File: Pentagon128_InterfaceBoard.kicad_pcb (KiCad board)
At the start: 2 copper layers, 150 x 121.6 mm, 40 parts, among them J1 DIN41612_02x32_AB, J10 Tape Out, J11 Tape In, J12 Mini-DIN-6, J14 Barrel_Jack_Switch, J2 Conn_02x03_Odd_Even ATmega Pr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, J3 Conn_02x08_Odd_Even Ext Keyb, J4 Conn_02x05_Odd_Even Kempston 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, J5 DE9_Plug Kempston Out SMD, J6 DE15_Plug_HighDensity VGA CRT, J7 Conn_01x04 FDD Power, J8 Conn_01x04 Audio In, J9 AudioJack3, Q1 Q_NPN_BCE, Q2 Q_NPN_BCE, Q3 Q_NPN_BCE, Q4 Q_NPN_BCE, U1 MT8816 PLCC44, U2 ATmega168PA-A

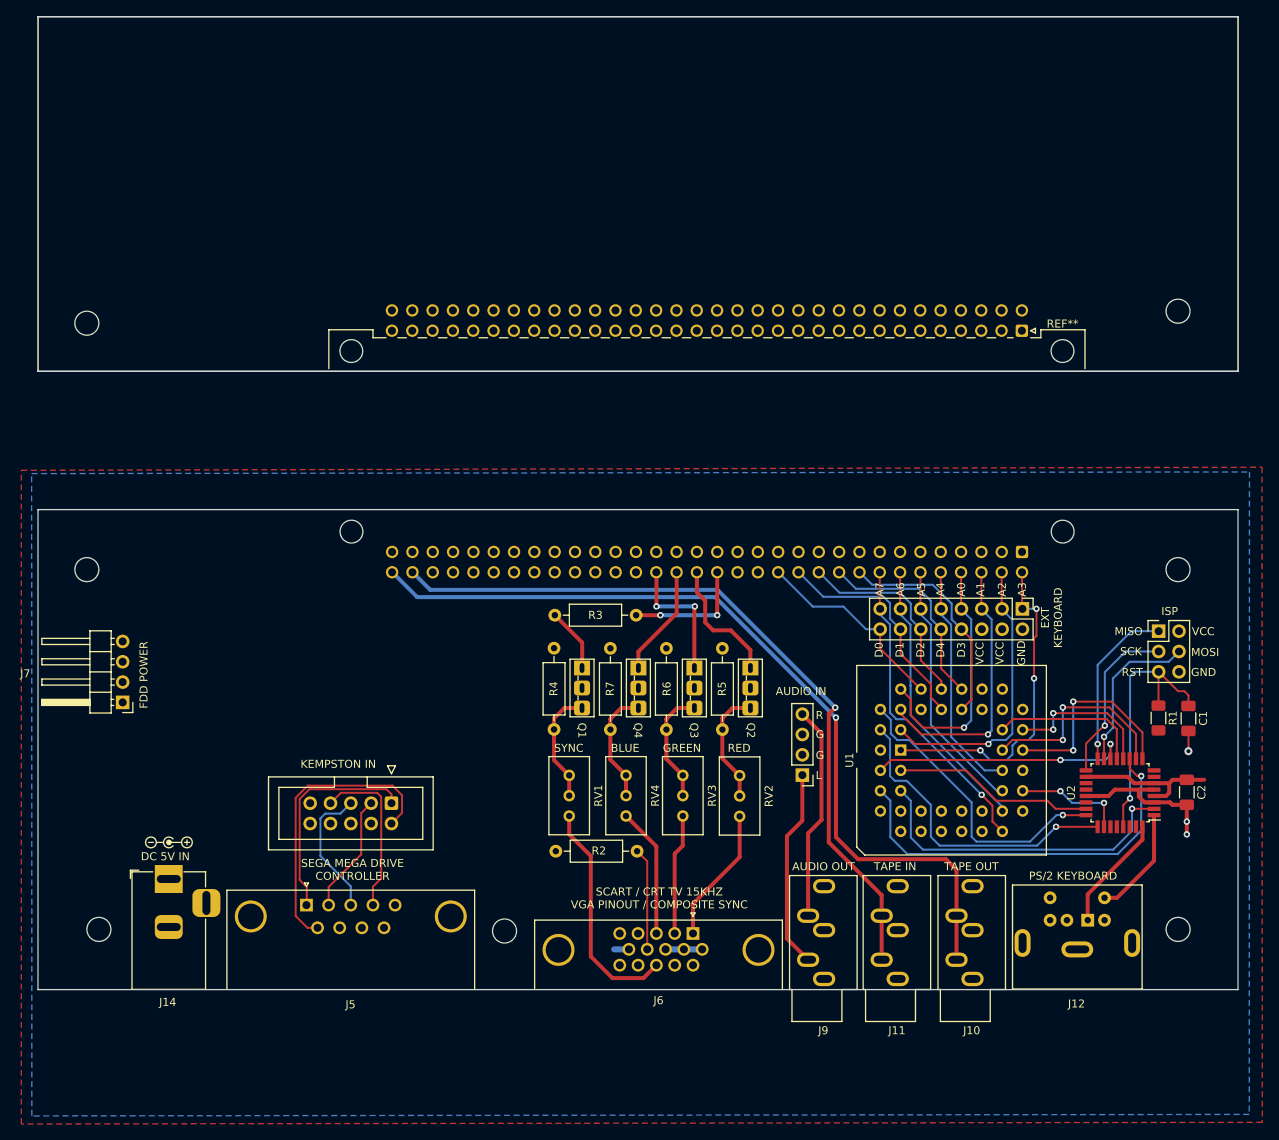
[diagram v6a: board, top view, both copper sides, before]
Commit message: Add VGA output based on @Alex_Eburg's https://github.com/AlexEkb4ever/ZX_RGBI2VGA-HDMI Repace Raspberry Pi Pico with RP2040-Zero. Add 9 pin RGBI header for Pentagon 2023. Add RP2040-Zero symbol and footprint.
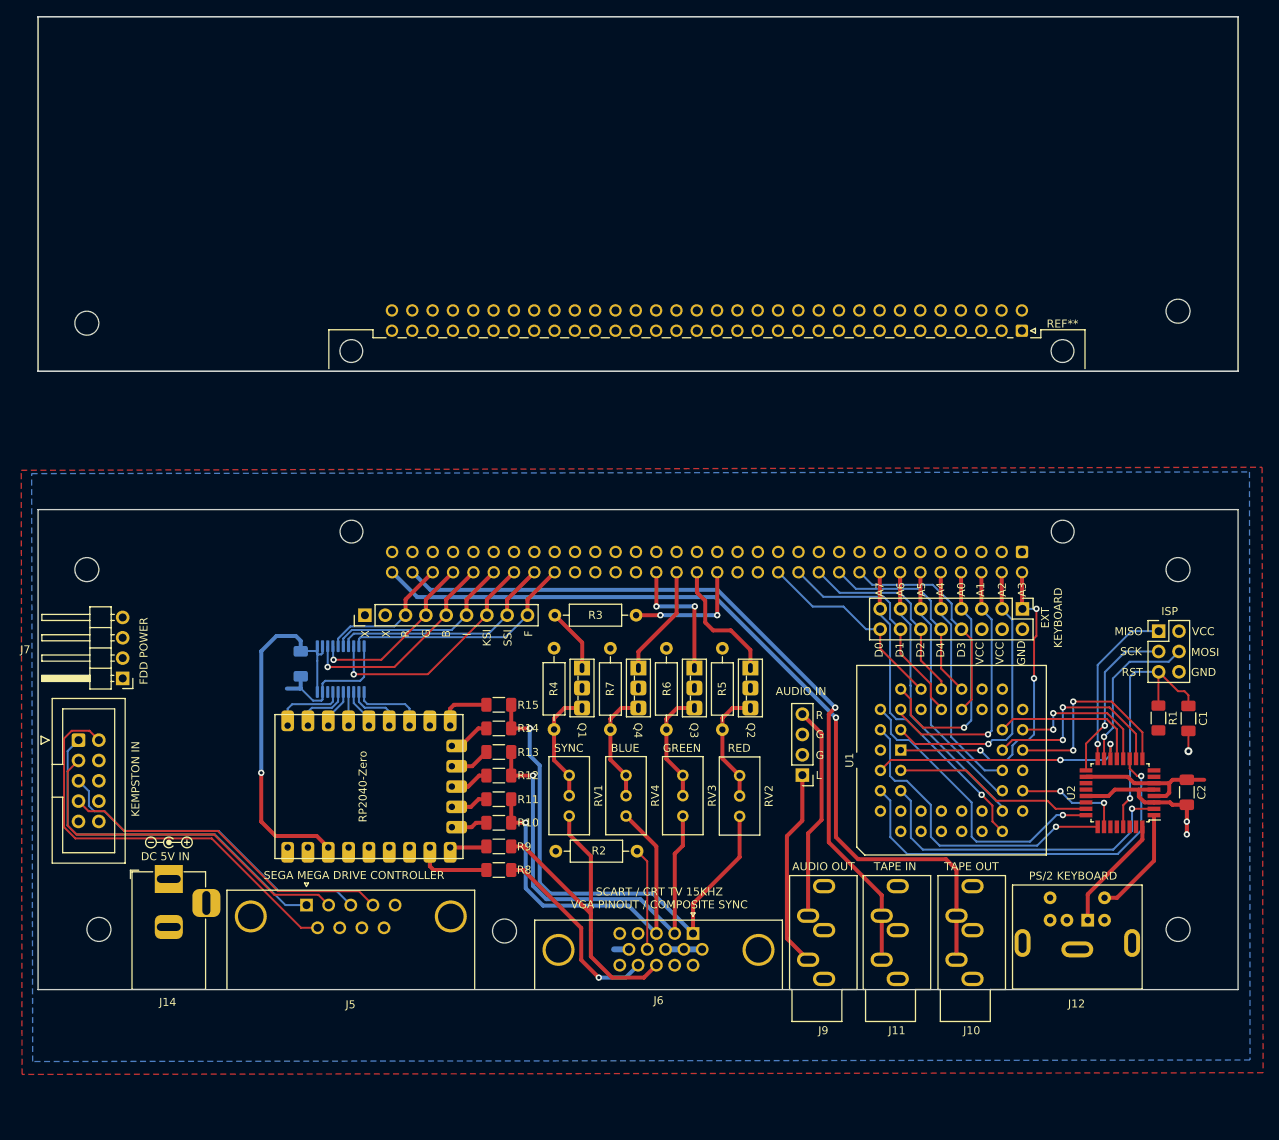
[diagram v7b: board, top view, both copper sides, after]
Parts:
- added C6: 0.1uF, Capacitor_SMD:C_1206_3216Metric_Pad1.33x1.80mm_HandSolder, B.Cu at (87.4, 77.6)
- added J15: Conn_01x07, Connector_PinHeader_2.54mm:PinHeader_1x09_P2.54mm_Vertical, F.Cu at (95.5, 71.5)
- added R10: 390, Resistor_SMD:R_1206_3216Metric_Pad1.30x1.75mm_HandSolder, F.Cu at (112.2, 97.5)
- added R11: 820, Resistor_SMD:R_1206_3216Metric_Pad1.30x1.75mm_HandSolder, F.Cu at (112.2, 94.5)
- added R12: 390, Resistor_SMD:R_1206_3216Metric_Pad1.30x1.75mm_HandSolder, F.Cu at (112.2, 91.5)
- added R13: 820, Resistor_SMD:R_1206_3216Metric_Pad1.30x1.75mm_HandSolder, F.Cu at (112.2, 88.6)
- added R14: 390, Resistor_SMD:R_1206_3216Metric_Pad1.30x1.75mm_HandSolder, F.Cu at (112.2, 85.7)
- added R15: 820, Resistor_SMD:R_1206_3216Metric_Pad1.30x1.75mm_HandSolder, F.Cu at (112.2, 82.7)
- added R8: 100, Resistor_SMD:R_1206_3216Metric_Pad1.30x1.75mm_HandSolder, F.Cu at (112.2, 103.3)
- added R9: 100, Resistor_SMD:R_1206_3216Metric_Pad1.30x1.75mm_HandSolder, F.Cu at (112.2, 100.4)
- added RZ1: RP2040-Zero, RP2040-Zero:RP2040-Zero, F.Cu at (108.7, 103.1)
- added U3: 74HC245, Package_SO:TSSOP-20_4.4x6.5mm_P0.65mm, B.Cu at (92.4, 78.2)
- moved J4 39.9 mm to (59.7, 87.1), turned to 0 degrees
- moved J7 3.00 mm to (65.2, 79.4)
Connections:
- net /CRT_BLUE renamed CRT_BLUE
- net /CRT_GREEN renamed CRT_GREEN
- net /CRT_RED renamed CRT_RED
- net /CRT_SYNC renamed CRT_SYNC
- J1 pad b24: unconnected-(J1-Pin_b24-Padb24) -> F
- J1 pad b25: unconnected-(J1-Pin_b25-Padb25) -> SSI
- J1 pad b26: unconnected-(J1-Pin_b26-Padb26) -> KSI
- J1 pad b27: unconnected-(J1-Pin_b27-Padb27) -> I
- J1 pad b28: unconnected-(J1-Pin_b28-Padb28) -> B
- J1 pad b29: unconnected-(J1-Pin_b29-Padb29) -> G
- J1 pad b30: unconnected-(J1-Pin_b30-Padb30) -> R
- J6 pad 14: unconnected-(J6-Pad14) -> CRT_VSYNC
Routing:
- net /pico RGB TO VGA/3V3: track 0.00 -> 47.8 mm, vias 0 -> 1
- net CRT_RED: track 17.1 -> 64.0 mm, vias 0 -> 1
- net CRT_GREEN: track 15.1 -> 54.8 mm, vias 0 -> 1
- net CRT_BLUE: track 16.2 -> 47.8 mm, vias 0 -> 1
- net /DOWN: track 14.9 -> 45.4 mm
- net KSI: track 0.00 -> 30.0 mm, vias 0 -> 1
- net F: track 0.00 -> 30.0 mm
- net SSI: track 0.00 -> 28.7 mm
- net B: track 0.00 -> 26.9 mm, vias 0 -> 1
- net /LEFT: track 17.0 -> 41.6 mm
- net CRT_VSYNC: track 0.00 -> 24.4 mm, vias 0 -> 1
- net I: track 0.00 -> 24.3 mm
- net G: track 0.00 -> 22.4 mm, vias 0 -> 1
- net /RIGHT: track 21.0 -> 42.2 mm
- net /UP: track 27.0 -> 45.3 mm
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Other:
- board text added: "B"
- board text added: "F"
- board text added: "I"
- board text added: "KSI"
- board text added: "SSI"
- board text added: "X"

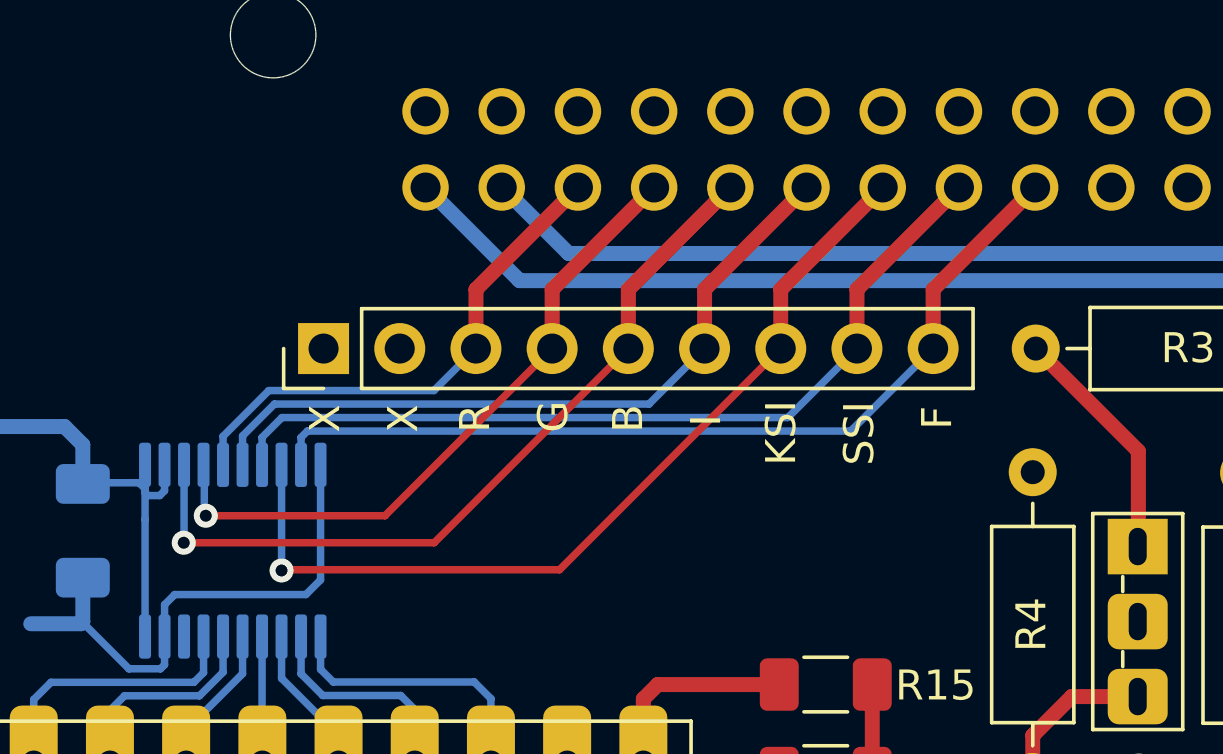
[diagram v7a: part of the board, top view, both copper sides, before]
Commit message: Add missing pico_RGB_TO_VGA.kicad_sch. Add 1 dummy pin to RGBI connector. Rename KSI -> KS, SSI -> SS.
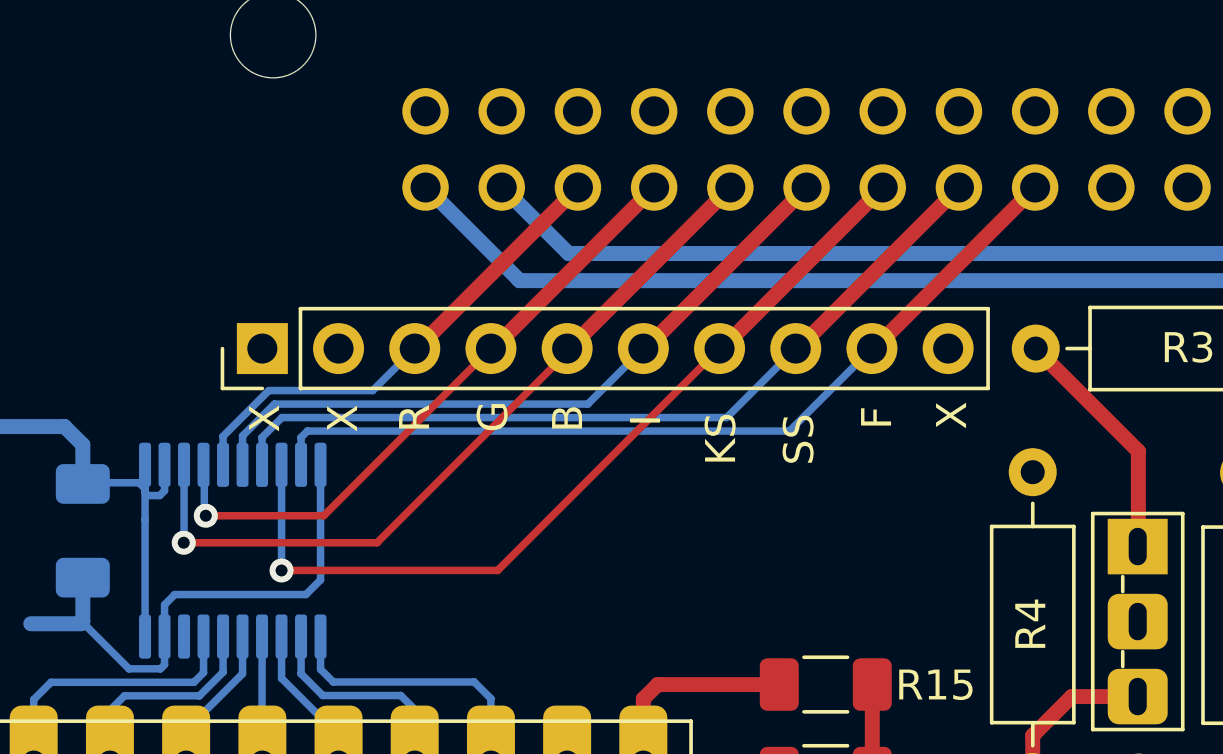
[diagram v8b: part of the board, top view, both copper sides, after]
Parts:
- J15: footprint Connector_PinHeader_2.54mm:PinHeader_1x09_P2.54mm_Vertical -> Connector_PinHeader_2.54mm:PinHeader_1x10_P2.54mm_Vertical
- moved J15 2.04 mm to (93.4, 71.5)
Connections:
- net KSI renamed KS
- net SSI renamed SS
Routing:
- net R: track 17.4 -> 16.2 mm
- net KS: track 30.0 -> 28.9 mm
- net I: track 24.3 -> 23.2 mm
- net G: track 22.4 -> 21.2 mm
- net F: track 30.0 -> 28.8 mm
- net SS: track 28.7 -> 27.6 mm
- net B: track 26.9 -> 25.8 mm
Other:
- board text added: "KS"
- board text added: "SS"
- board text removed: "KSI"
- board text removed: "SSI"
